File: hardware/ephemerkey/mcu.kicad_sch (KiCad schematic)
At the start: 24 parts, among them J1 SWD TC2030-NL, J2 LOCK IF (I2C JST-PH), SW1 USER1, SW2 USER2, SW3 USER3/DFU, U1 STM32U083KCU6, Y1 32.768kHz

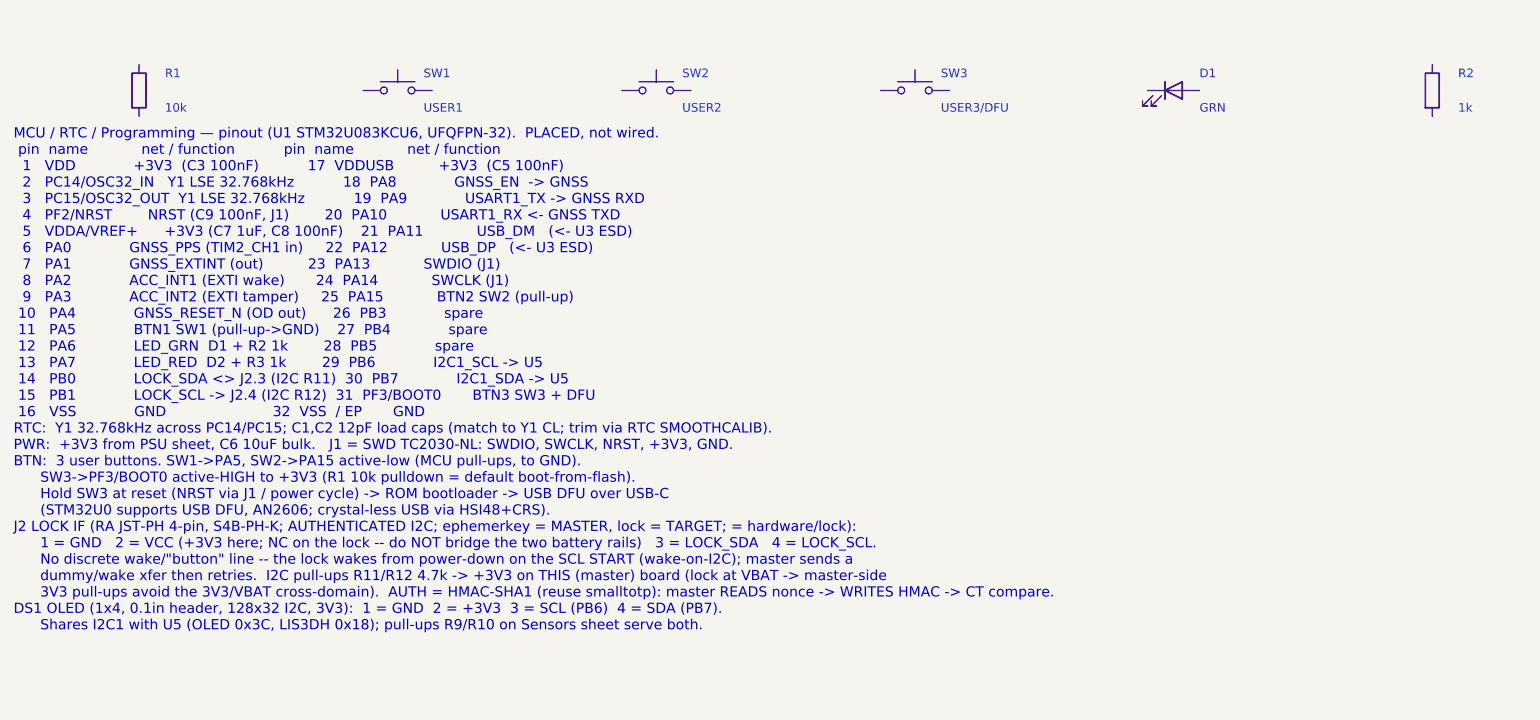
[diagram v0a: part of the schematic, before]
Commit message: lock: second servo output, clearer wiring notes, start PCB layout
- Add a second servo output (J8 + SERVO_SIG2 on PB4, R24/R25) sharing the
  VSERVO rail and the load-switch/interlock -- e.g. a dual-latch lock.
- Rewrite the per-sheet wiring notes (MCU/PWR/DRV) from prose into terse
  pin -> net maps: one line per part, every pin = its net, with a NETS IN
  header for cross-sheet signals. Rationale stays in the README.
- kschgen: park the wiring note below all placed components so the text no
  longer overlaps symbols (computed from the last component row).
- Start the lock PCB layout (hardware/lock/lock.kicad_pcb).

Board regenerates + checks clean (49 components; all footprints carry 3D models).

Co-Authored-By: Claude Opus 4.8 (1M context) <noreply@anthropic.com>
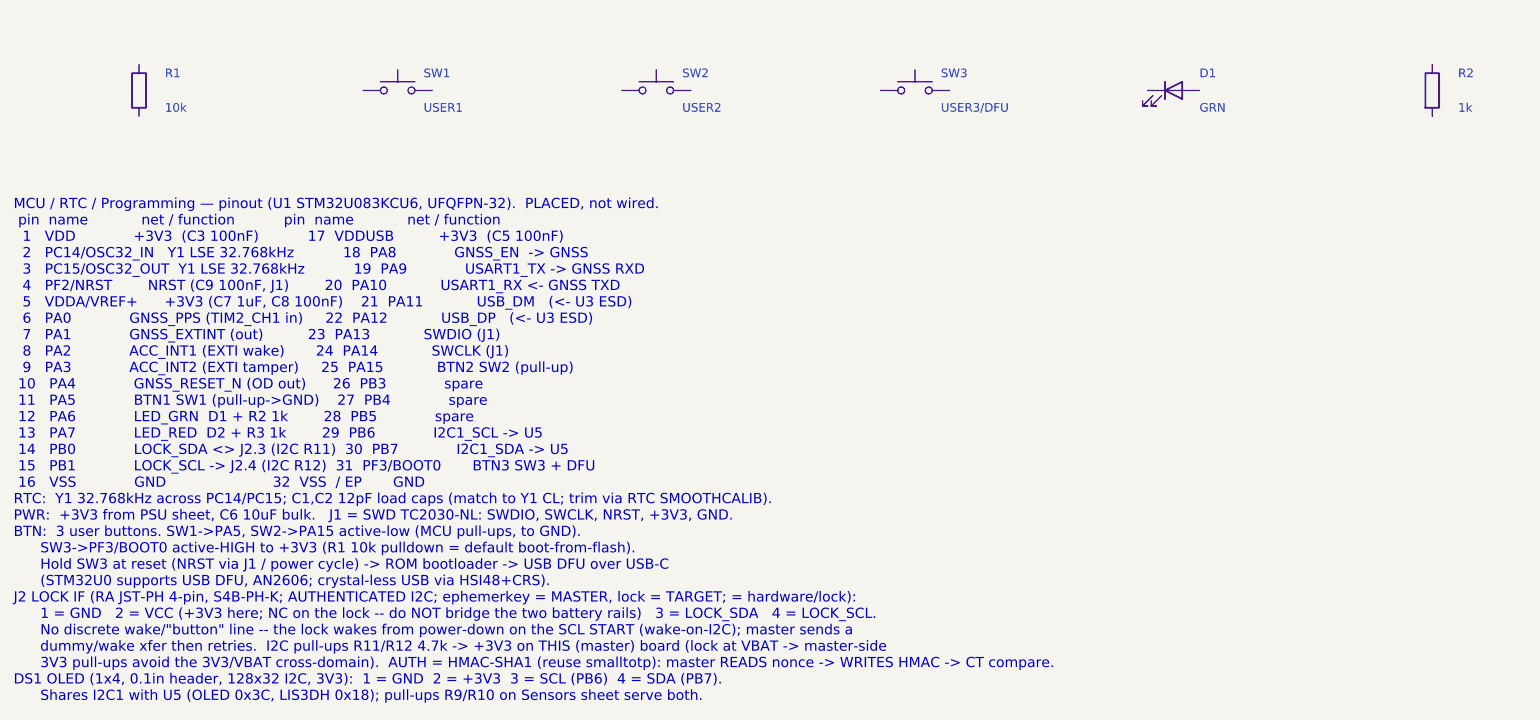
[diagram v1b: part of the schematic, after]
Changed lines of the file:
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@@
 		(instances
 			(project "ephemerkey"
-				(path "/e1000000-0000-4000-8000-000000000001/99835d2b-2153-4c30-83c1-e688c6f70aff"
+				(path "/e1000000-0000-4000-8000-000000000001/cc272c1a-e675-41e8-b312-d63babb90e3e"
 					(reference "U1")
 					(unit 1)
@@
 		(instances
 			(project "ephemerkey"
-				(path "/e1000000-0000-4000-8000-000000000001/99835d2b-2153-4c30-83c1-e688c6f70aff"
+				(path "/e1000000-0000-4000-8000-000000000001/cc272c1a-e675-41e8-b312-d63babb90e3e"
 					(reference "J1")
 					(unit 1)
@@
 		(instances
 			(project "ephemerkey"
-				(path "/e1000000-0000-4000-8000-000000000001/99835d2b-2153-4c30-83c1-e688c6f70aff"
+				(path "/e1000000-0000-4000-8000-000000000001/cc272c1a-e675-41e8-b312-d63babb90e3e"
 					(reference "J2")
 					(unit 1)
@@
 		(instances
 			(project "ephemerkey"
-				(path "/e1000000-0000-4000-8000-000000000001/99835d2b-2153-4c30-83c1-e688c6f70aff"
+				(path "/e1000000-0000-4000-8000-000000000001/cc272c1a-e675-41e8-b312-d63babb90e3e"
 					(reference "DS1")
 					(unit 1)
@@
 		(instances
 			(project "ephemerkey"
-				(path "/e1000000-0000-4000-8000-000000000001/99835d2b-2153-4c30-83c1-e688c6f70aff"
+				(path "/e1000000-0000-4000-8000-000000000001/cc272c1a-e675-41e8-b312-d63babb90e3e"
 					(reference "Y1")
 					(unit 1)
@@
 		(instances
 			(project "ephemerkey"
-				(path "/e1000000-0000-4000-8000-000000000001/99835d2b-2153-4c30-83c1-e688c6f70aff"
+				(path "/e1000000-0000-4000-8000-000000000001/cc272c1a-e675-41e8-b312-d63babb90e3e"
 					(reference "C1")
 					(unit 1)
@@
 		(instances
 			(project "ephemerkey"
-				(path "/e1000000-0000-4000-8000-000000000001/99835d2b-2153-4c30-83c1-e688c6f70aff"
+				(path "/e1000000-0000-4000-8000-000000000001/cc272c1a-e675-41e8-b312-d63babb90e3e"
 					(reference "C2")
 					(unit 1)
@@
 		(instances
 			(project "ephemerkey"
-				(path "/e1000000-0000-4000-8000-000000000001/99835d2b-2153-4c30-83c1-e688c6f70aff"
+				(path "/e1000000-0000-4000-8000-000000000001/cc272c1a-e675-41e8-b312-d63babb90e3e"
 					(reference "C3")
 					(unit 1)
@@
 		(instances
 			(project "ephemerkey"
-				(path "/e1000000-0000-4000-8000-000000000001/99835d2b-2153-4c30-83c1-e688c6f70aff"
+				(path "/e1000000-0000-4000-8000-000000000001/cc272c1a-e675-41e8-b312-d63babb90e3e"
 					(reference "C4")
 					(unit 1)
@@
 		(instances
 			(project "ephemerkey"
-				(path "/e1000000-0000-4000-8000-000000000001/99835d2b-2153-4c30-83c1-e688c6f70aff"
+				(path "/e1000000-0000-4000-8000-000000000001/cc272c1a-e675-41e8-b312-d63babb90e3e"
 					(reference "C5")
 					(unit 1)
@@
 		(instances
 			(project "ephemerkey"
-				(path "/e1000000-0000-4000-8000-000000000001/99835d2b-2153-4c30-83c1-e688c6f70aff"
+				(path "/e1000000-0000-4000-8000-000000000001/cc272c1a-e675-41e8-b312-d63babb90e3e"
 					(reference "C6")
 					(unit 1)
@@
 		(instances
 			(project "ephemerkey"
-				(path "/e1000000-0000-4000-8000-000000000001/99835d2b-2153-4c30-83c1-e688c6f70aff"
+				(path "/e1000000-0000-4000-8000-000000000001/cc272c1a-e675-41e8-b312-d63babb90e3e"
 					(reference "C7")
 					(unit 1)
@@
 		(instances
 			(project "ephemerkey"
-				(path "/e1000000-0000-4000-8000-000000000001/99835d2b-2153-4c30-83c1-e688c6f70aff"
+				(path "/e1000000-0000-4000-8000-000000000001/cc272c1a-e675-41e8-b312-d63babb90e3e"
 					(reference "C8")
 					(unit 1)
@@
 		(instances
 			(project "ephemerkey"
-				(path "/e1000000-0000-4000-8000-000000000001/99835d2b-2153-4c30-83c1-e688c6f70aff"
+				(path "/e1000000-0000-4000-8000-000000000001/cc272c1a-e675-41e8-b312-d63babb90e3e"
 					(reference "C9")
 					(unit 1)
@@
 		(instances
 			(project "ephemerkey"
-				(path "/e1000000-0000-4000-8000-000000000001/99835d2b-2153-4c30-83c1-e688c6f70aff"
+				(path "/e1000000-0000-4000-8000-000000000001/cc272c1a-e675-41e8-b312-d63babb90e3e"
 					(reference "R1")
 					(unit 1)
@@
 		(instances
 			(project "ephemerkey"
-				(path "/e1000000-0000-4000-8000-000000000001/99835d2b-2153-4c30-83c1-e688c6f70aff"
+				(path "/e1000000-0000-4000-8000-000000000001/cc272c1a-e675-41e8-b312-d63babb90e3e"
 					(reference "SW1")
 					(unit 1)
@@
 		(instances
 			(project "ephemerkey"
-				(path "/e1000000-0000-4000-8000-000000000001/99835d2b-2153-4c30-83c1-e688c6f70aff"
+				(path "/e1000000-0000-4000-8000-000000000001/cc272c1a-e675-41e8-b312-d63babb90e3e"
 					(reference "SW2")
 					(unit 1)
@@
 		(instances
 			(project "ephemerkey"
-				(path "/e1000000-0000-4000-8000-000000000001/99835d2b-2153-4c30-83c1-e688c6f70aff"
+				(path "/e1000000-0000-4000-8000-000000000001/cc272c1a-e675-41e8-b312-d63babb90e3e"
 					(reference "SW3")
 					(unit 1)
@@
 		(instances
 			(project "ephemerkey"
-				(path "/e1000000-0000-4000-8000-000000000001/99835d2b-2153-4c30-83c1-e688c6f70aff"
+				(path "/e1000000-0000-4000-8000-000000000001/cc272c1a-e675-41e8-b312-d63babb90e3e"
 					(reference "D1")
 					(unit 1)
@@
 		(instances
 			(project "ephemerkey"
-				(path "/e1000000-0000-4000-8000-000000000001/99835d2b-2153-4c30-83c1-e688c6f70aff"
+				(path "/e1000000-0000-4000-8000-000000000001/cc272c1a-e675-41e8-b312-d63babb90e3e"
 					(reference "R2")
 					(unit 1)
@@
 		(instances
 			(project "ephemerkey"
-				(path "/e1000000-0000-4000-8000-000000000001/99835d2b-2153-4c30-83c1-e688c6f70aff"
+				(path "/e1000000-0000-4000-8000-000000000001/cc272c1a-e675-41e8-b312-d63babb90e3e"
 					(reference "D2")
 					(unit 1)
@@
 		(instances
 			(project "ephemerkey"
-				(path "/e1000000-0000-4000-8000-000000000001/99835d2b-2153-4c30-83c1-e688c6f70aff"
+				(path "/e1000000-0000-4000-8000-000000000001/cc272c1a-e675-41e8-b312-d63babb90e3e"
 					(reference "R3")
 					(unit 1)
@@
 		(instances
 			(project "ephemerkey"
-				(path "/e1000000-0000-4000-8000-000000000001/99835d2b-2153-4c30-83c1-e688c6f70aff"
+				(path "/e1000000-0000-4000-8000-000000000001/cc272c1a-e675-41e8-b312-d63babb90e3e"
 					(reference "R11")
 					(unit 1)
@@
 		(instances
 			(project "ephemerkey"
-				(path "/e1000000-0000-4000-8000-000000000001/99835d2b-2153-4c30-83c1-e688c6f70aff"
+				(path "/e1000000-0000-4000-8000-000000000001/cc272c1a-e675-41e8-b312-d63babb90e3e"
 					(reference "R12")
 					(unit 1)
@@
 	(text "MCU / RTC / Programming — pinout (U1 STM32U083KCU6, UFQFPN-32).  PLACED, not wired.\n pin  name            net / function           pin  name            net / function\n  1   VDD             +3V3  (C3 100nF)           17  VDDUSB          +3V3  (C5 100nF)\n  2   PC14/OSC32_IN   Y1 LSE 32.768kHz           18  PA8             GNSS_EN  -> GNSS\n  3   PC15/OSC32_OUT  Y1 LSE 32.768kHz           19  PA9             USART1_TX -> GNSS RXD\n  4   PF2/NRST        NRST (C9 100nF, J1)        20  PA10            USART1_RX <- GNSS TXD\n  5   VDDA/VREF+      +3V3 (C7 1uF, C8 100nF)    21  PA11            USB_DM   (<- U3 ESD)\n  6   PA0             GNSS_PPS (TIM2_CH1 in)     22  PA12            USB_DP   (<- U3 ESD)\n  7   PA1             GNSS_EXTINT (out)          23  PA13            SWDIO (J1)\n  8   PA2             ACC_INT1 (EXTI wake)       24  PA14            SWCLK (J1)\n  9   PA3             ACC_INT2 (EXTI tamper)     25  PA15            BTN2 SW2 (pull-up)\n 10   PA4             GNSS_RESET_N (OD out)      26  PB3             spare\n 11   PA5             BTN1 SW1 (pull-up->GND)    27  PB4             spare\n 12   PA6             LED_GRN  D1 + R2 1k        28  PB5             spare\n 13   PA7             LED_RED  D2 + R3 1k        29  PB6             I2C1_SCL -> U5\n 14   PB0             LOCK_SDA <> J2.3 (I2C R11)  30  PB7             I2C1_SDA -> U5\n 15   PB1             LOCK_SCL -> J2.4 (I2C R12)  31  PF3/BOOT0       BTN3 SW3 + DFU\n 16   VSS             GND                        32  VSS  / EP       GND\nRTC:  Y1 32.768kHz across PC14/PC15; C1,C2 12pF load caps (match to Y1 CL; trim via RTC SMOOTHCALIB).\nPWR:  +3V3 from PSU sheet, C6 10uF bulk.   J1 = SWD TC2030-NL: SWDIO, SWCLK, NRST, +3V3, GND.\nBTN:  3 user buttons. SW1->PA5, SW2->PA15 active-low (MCU pull-ups, to GND).\n      SW3->PF3/BOOT0 active-HIGH to +3V3 (R1 10k pulldown = default boot-from-flash).\n      Hold SW3 at reset (NRST via J1 / power cycle) -> ROM bootloader -> USB DFU over USB-C\n      (STM32U0 supports USB DFU, AN2606; crystal-less USB via HSI48+CRS).\nJ2 LOCK IF (RA JST-PH 4-pin, S4B-PH-K; AUTHENTICATED I2C; ephemerkey = MASTER, lock = TARGET; = hardware/lock):\n      1 = GND   2 = VCC (+3V3 here; NC on the lock -- do NOT bridge the two battery rails)   3 = LOCK_SDA   4 = LOCK_SCL.\n      No discrete wake/\"button\" line -- the lock wakes from power-down on the SCL START (wake-on-I2C); master sends a\n      dummy/wake xfer then retries.  I2C pull-ups R11/R12 4.7k -> +3V3 on THIS (master) board (lock at VBAT -> master-side\n      3V3 pull-ups avoid the 3V3/VBAT cross-domain).  AUTH = HMAC-SHA1 (reuse smalltotp): master READS nonce -> WRITES HMAC -> CT compare.\nDS1 OLED (1x4, 0.1in header, 128x32 I2C, 3V3):  1 = GND  2 = +3V3  3 = SCL (PB6)  4 = SDA (PB7).\n      Shares I2C1 with U5 (OLED 0x3C, LIS3DH 0x18); pull-ups R9/R10 on Sensors sheet serve both."
 		(exclude_from_sim no)
-		(at 12.00 158.00 0)
+		(at 12.00 168.40 0)
 		(effects (font (size 1.5 1.5)) (justify left top))
 	)

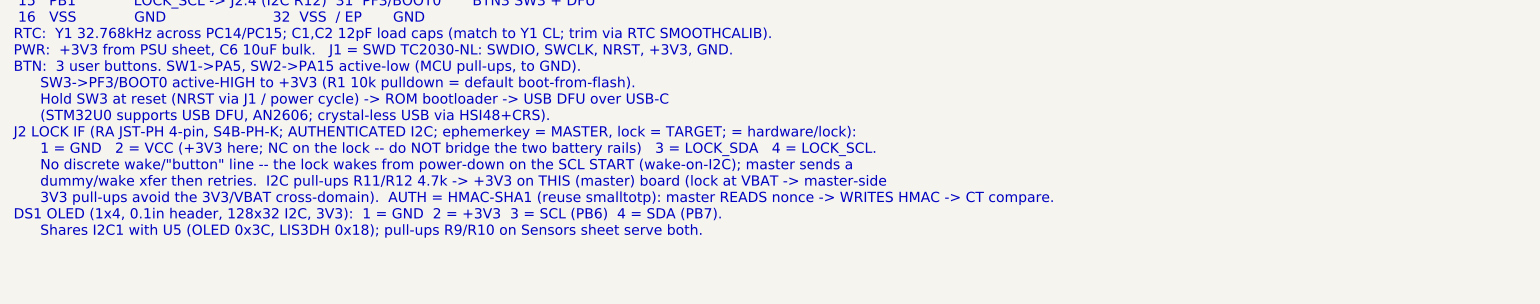
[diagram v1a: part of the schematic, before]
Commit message: lock: power from I2C connector (VSYS), LED on PC3; route board; ephemerkey J2=VSYS
Power move: the lock has NO local battery (J1 removed) — VCC and the boost/
actuator draw come from ephemerkey's VSYS rail over the I2C connector (J2.2).
- ephemerkey: J2.2 = VSYS (was +3V3); manifest note + DESIGN.md updated, regenerated.
- lock: README interface/architecture/BOM + servo source (R13=VSOL / R14=VSYS,
  no more VBAT) updated to match the as-wired board.
- Caveat documented: a 12V solenoid pull-in (~3-4A) exceeds a JST-PH contact and
  ephemerkey's load-share; favor the 6V servo / low-duty, or a dedicated feed.
- I2C pull-ups stay on ephemerkey at +3V3 (STM32 pins not >3.6V tolerant).

LED move: status LED (D1) is driven by PC3, not PA3 (PA3 now spare). Docs + manifest.

lock schematic + PCB are now hand-wired and fully routed (DRC: 0 unconnected,
0 schematic-parity). Manifest marked REFERENCE-OF-RECORD — do not regenerate
(would destroy the wiring). Verified with KiCad's own kicad-cli ERC/DRC.

Pending (owner fixing): PWR_FLAGs on VCC/GND, NC flags on unused pins, J6/J7 GND
thermal relief, minor stub/silk cleanups.

Co-Authored-By: Claude Opus 4.8 (1M context) <noreply@anthropic.com>
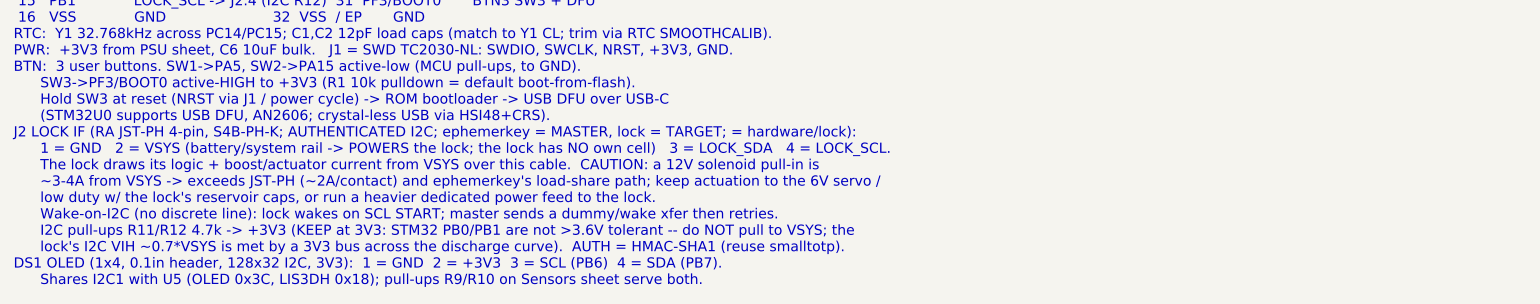
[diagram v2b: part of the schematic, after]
